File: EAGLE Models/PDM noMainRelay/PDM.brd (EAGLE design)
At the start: 89.7 x 75.6 mm, 20 parts

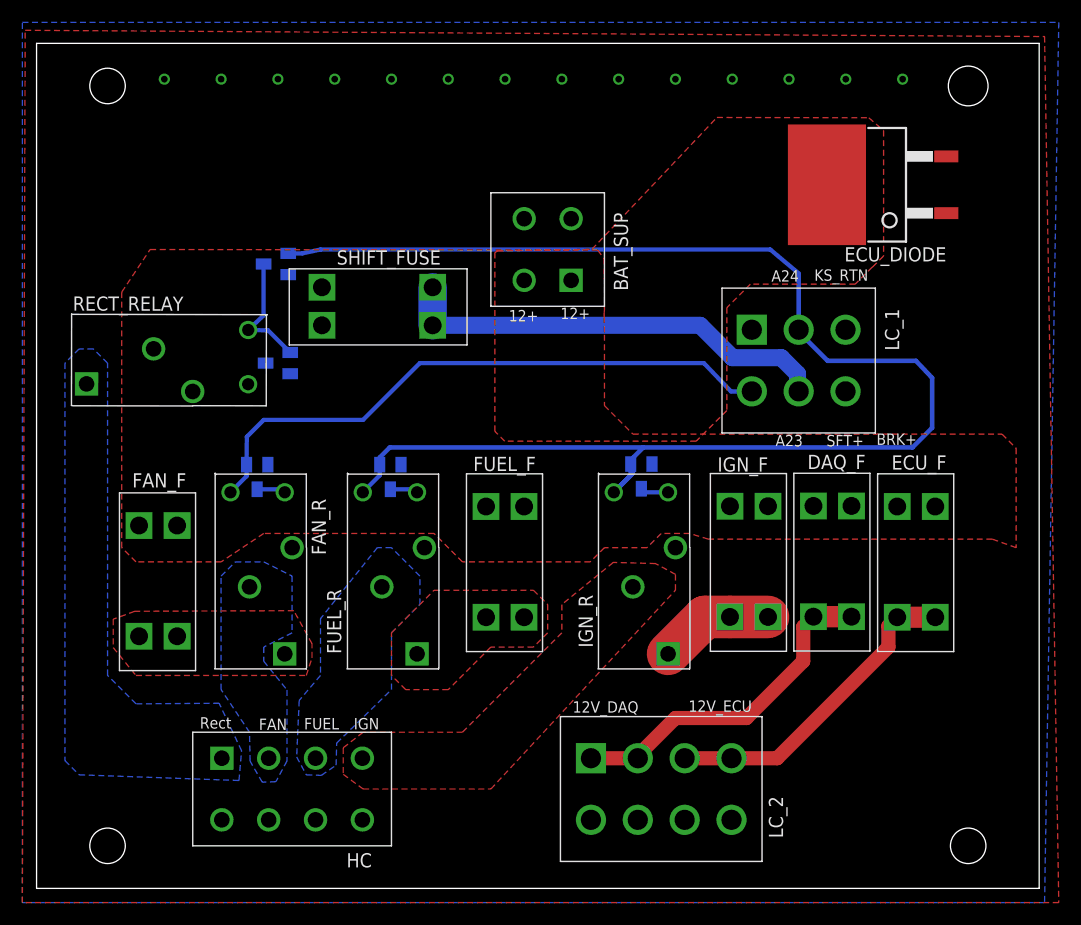
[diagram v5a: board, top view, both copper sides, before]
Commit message: Moved diode
Added different diode
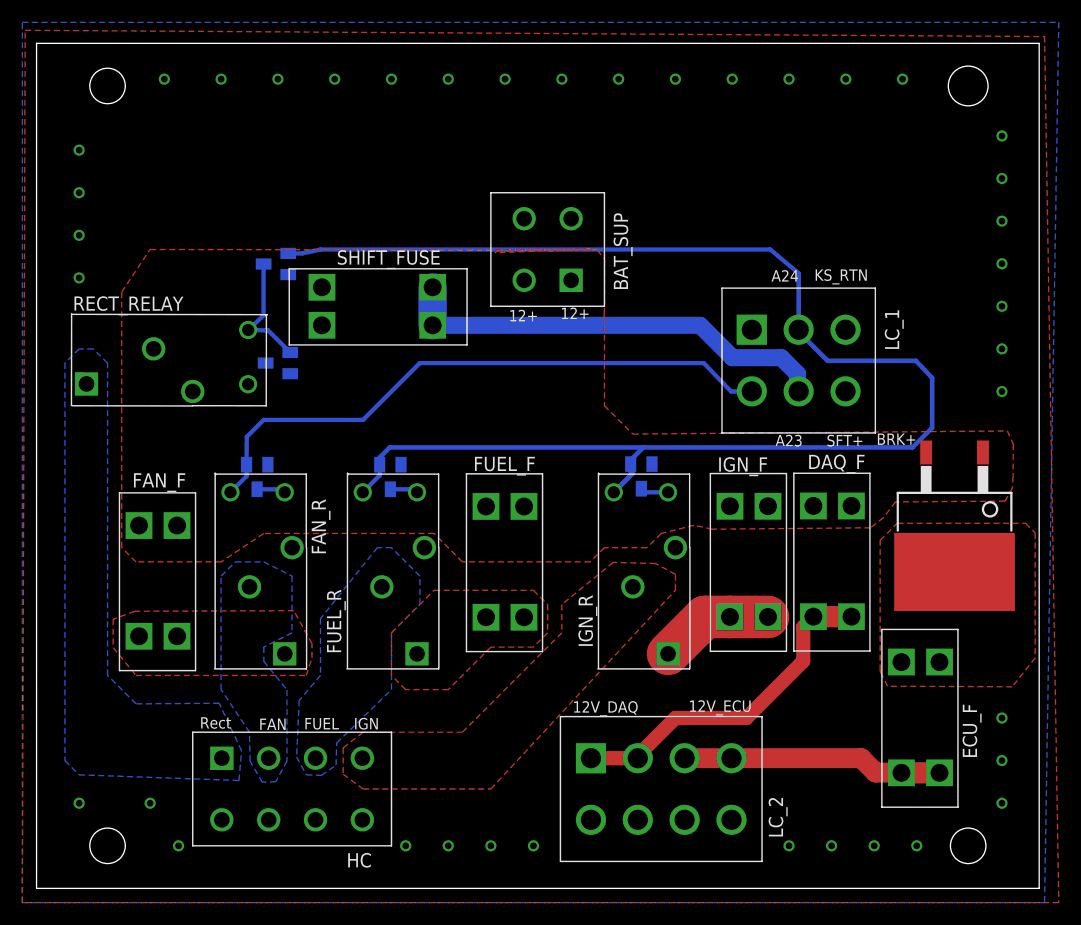
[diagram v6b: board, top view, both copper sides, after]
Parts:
- removed ECU_DIODE: VBT2045BP-E3, vishay:TO-263-3
- added U$1: STPS20L15G-TRTO, st-microelectronics:TO-262DIODE
- moved ECU_F 13.9 mm to (79.1, 15.3)
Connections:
- new net ECU_PROTECTED: ECU_F.1, ECU_F.2, U$1.K
- net 12V: now also U$1.1, U$1.2; no longer ECU_DIODE.K, ECU_F.1, ECU_F.2
- net GND: no longer ECU_DIODE.1, ECU_DIODE.2
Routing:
- net 12V_FUSED_ECU: track 28.7 -> 23.3 mm
- added copper zone on layer 1, net ECU_PROTECTED
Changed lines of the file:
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@@
 <param name="mdViaViaSameLayer" value="8mil"/>
 <param name="mnLayersViaInSmd" value="2"/>
-<param name="mdCopperDimension" value="40mil"/>
+<param name="mdCopperDimension" value="10mil"/>
 <param name="mdDrill" value="8mil"/>
 <param name="mdSmdStop" value="0mil"/>
 <param name="msWidth" value="10mil"/>
-<param name="msDrill" value="20mil"/>
+<param name="msDrill" value="15mil"/>
 <param name="msMicroVia" value="9.99mm"/>
 <param name="msBlindViaRatio" value="0.5"/>
@@
 <element name="IGN_F" library="Keystone" package="3568" value="3568" x="63.7286" y="29.2354" smashed="yes" rot="R270">
 <attribute name="NAME" x="60.9092" y="37.2872" size="1.27" layer="25"/>
-<attribute name="VALUE" x="61.3664" y="31.3436" size="1.27" layer="27"/>
+<attribute name="VALUE" x="61.3918" y="30.6324" size="1.27" layer="27"/>
 </element>
 <element name="FAN_F" library="Keystone" package="3568" value="3568" x="10.8712" y="27.5082" smashed="yes" rot="R270">
@@
 <element name="DAQ_F" library="Keystone" package="3568" value="3568" x="71.1962" y="29.2608" smashed="yes" rot="R270">
 <attribute name="NAME" x="68.961" y="37.5158" size="1.27" layer="25"/>
-<attribute name="VALUE" x="69.5452" y="31.4198" size="1.27" layer="27"/>
+<attribute name="VALUE" x="69.5198" y="31.1912" size="1.27" layer="27"/>
 </element>
 <element name="LC_1" library="BMS Lbr" package="1586041-6" value="1586041-6" x="68.1736" y="47.2186" smashed="yes">
@@
 </element>
 <element name="IGN_D" library="diodes-inc" package="SOT23-3" value="MMBD4448H-7-F" x="54.102" y="36.8554" smashed="yes" rot="MR180">
-<attribute name="NAME" x="51.816" y="40.4368" size="1.27" layer="26" rot="MR180"/>
+<attribute name="NAME" x="51.7652" y="41.6052" size="1.27" layer="26" rot="MR180"/>
 </element>
 <element name="FUEL_D" library="diodes-inc" package="SOT23-3" value="MMBD4448H-7-F" x="31.6484" y="36.8046" smashed="yes" rot="MR180">
-<attribute name="NAME" x="28.3464" y="40.3352" size="1.27" layer="26" rot="MR180"/>
+<attribute name="NAME" x="28.5242" y="40.7162" size="1.27" layer="26" rot="MR180"/>
 </element>
 <element name="FAN_D" library="diodes-inc" package="SOT23-3" value="MMBD4448H-7-F" x="19.7358" y="36.8046" smashed="yes" rot="MR180">
-<attribute name="NAME" x="17.4244" y="40.3352" size="1.27" layer="26" rot="MR180"/>
-</element>
-<element name="ECU_F" library="Keystone" package="3568" value="3568" x="78.6892" y="29.21" smashed="yes" rot="R270">
-<attribute name="NAME" x="76.4794" y="37.465" size="1.27" layer="25"/>
-<attribute name="VALUE" x="77.1398" y="31.3436" size="1.27" layer="27"/>
+<attribute name="NAME" x="17.2974" y="41.2242" size="1.27" layer="26" rot="MR180"/>
+</element>
+<element name="ECU_F" library="Keystone" package="3568" value="3568" x="79.0702" y="15.2908" smashed="yes" rot="R270">
+<attribute name="NAME" x="84.1248" y="11.6078" size="1.27" layer="25" rot="R90"/>
+<attribute name="VALUE" x="77.3684" y="15.5194" size="1.27" layer="27"/>
 </element>
 <element name="CC_D" library="diodes-inc" package="SOT23-3" value="MMBD4448H-7-F" x="21.59" y="46.99" smashed="yes" rot="MR270">
 <attribute name="NAME" x="25.5778" y="48.3108" size="1.27" layer="26" rot="MR270"/>
 </element>
-<element name="ECU_DIODE" library="vishay" package="TO-263-3" value="VBT2045BP-E3" x="76.3016" y="62.9412" rot="R90"/>
+<element name="U$1" library="st-microelectronics" package="TO-262DIODE" value="STPS20L15G-TRTO" x="82.1182" y="33.909" smashed="yes" rot="R180"/>
 </elements>
 <signals>
@@
 <via x="77.47" y="72.39" extent="1-16" drill="0.6"/>
 <contactref element="CC_D" pad="3"/>
-<contactref element="ECU_DIODE" pad="1"/>
-<contactref element="ECU_DIODE" pad="2"/>
+<via x="86.36" y="44.45" extent="1-16" drill="0.6"/>
+<via x="86.36" y="48.26" extent="1-16" drill="0.6"/>
+<via x="86.36" y="52.07" extent="1-16" drill="0.6"/>
+<via x="86.36" y="55.88" extent="1-16" drill="0.6"/>
+<via x="86.36" y="59.69" extent="1-16" drill="0.6"/>
+<via x="86.36" y="15.24" extent="1-16" drill="0.6"/>
+<via x="86.36" y="11.43" extent="1-16" drill="0.6"/>
+<via x="74.93" y="3.81" extent="1-16" drill="0.6"/>
+<via x="71.12" y="3.81" extent="1-16" drill="0.6"/>
+<via x="67.31" y="3.81" extent="1-16" drill="0.6"/>
+<via x="44.45" y="3.81" extent="1-16" drill="0.6"/>
+<via x="40.64" y="3.81" extent="1-16" drill="0.6"/>
+<via x="36.83" y="3.81" extent="1-16" drill="0.6"/>
+<via x="33.02" y="3.81" extent="1-16" drill="0.6"/>
+<via x="12.7" y="3.81" extent="1-16" drill="0.6"/>
+<via x="10.16" y="7.62" extent="1-16" drill="0.6"/>
+<via x="3.81" y="7.62" extent="1-16" drill="0.6"/>
+<via x="86.36" y="7.62" extent="1-16" drill="0.6"/>
+<via x="78.74" y="3.81" extent="1-16" drill="0.6"/>
+<via x="3.81" y="66.04" extent="1-16" drill="0.6"/>
+<via x="3.81" y="62.23" extent="1-16" drill="0.6"/>
+<via x="3.81" y="58.42" extent="1-16" drill="0.6"/>
+<via x="3.81" y="54.61" extent="1-16" drill="0.6"/>
+<via x="86.36" y="63.5" extent="1-16" drill="0.6"/>
+<via x="86.36" y="67.31" extent="1-16" drill="0.6"/>
 </signal>
 <signal name="12V">
@@
 <contactref element="FUEL_D" pad="3"/>
 <contactref element="FAN_D" pad="3"/>
-<contactref element="ECU_F" pad="2"/>
-<contactref element="ECU_F" pad="1"/>
 <wire x1="22.1996" y1="35.433" x2="22.1996" y2="35.8726" width="0.381" layer="16"/>
 <wire x1="54.102" y1="35.7554" x2="54.4244" y2="35.433" width="0.381" layer="16"/>
@@
 <vertex x="10.16" y="57.15"/>
 <vertex x="50.1904" y="57.0992"/>
-<vertex x="50.7746" y="56.3372"/>
+<vertex x="50.8254" y="56.2102"/>
 <vertex x="50.8" y="51.7652"/>
 <vertex x="50.7746" y="51.5112"/>
@@
 <vertex x="50.8" y="43.18"/>
 <vertex x="53.34" y="40.64"/>
-<vertex x="86.36" y="40.64"/>
-<vertex x="87.63" y="39.37"/>
-<vertex x="87.63" y="30.48"/>
-<vertex x="85.4964" y="31.242"/>
-<vertex x="60.0964" y="31.242"/>
-<vertex x="58.42" y="31.75"/>
+<vertex x="86.8426" y="40.9194"/>
+<vertex x="87.376" y="39.7256"/>
+<vertex x="87.3506" y="36.83"/>
+<vertex x="87.2998" y="35.8394"/>
+<vertex x="86.6394" y="34.6456"/>
+<vertex x="76.835" y="34.5694"/>
+<vertex x="75.7682" y="33.1724"/>
+<vertex x="74.5998" y="32.258"/>
+<vertex x="60.4266" y="32.131"/>
+<vertex x="58.8264" y="32.4866"/>
 <vertex x="55.88" y="31.75"/>
 <vertex x="54.61" y="30.48"/>
@@
 </polygon>
 <wire x1="42.9973" y1="54.3941" x2="43.61941875" y2="54.3941" width="0.4064" layer="1"/>
-<contactref element="ECU_DIODE" pad="K"/>
 <polygon width="0.4064" layer="1">
 <vertex x="41.2242" y="57.023"/>
 <vertex x="49.6824" y="57.1754"/>
-<vertex x="60.8584" y="68.961"/>
-<vertex x="74.4474" y="68.9356"/>
-<vertex x="75.7682" y="67.7926"/>
-<vertex x="75.7682" y="56.5658"/>
-<vertex x="74.7776" y="55.5752"/>
-<vertex x="74.7522" y="55.5752"/>
-<vertex x="73.2282" y="54.0512"/>
-<vertex x="63.8556" y="54.0512"/>
-<vertex x="61.7474" y="51.943"/>
-<vertex x="61.7474" y="42.7482"/>
-<vertex x="59.0042" y="40.005"/>
-<vertex x="41.8846" y="40.005"/>
-<vertex x="40.9956" y="40.894"/>
 <vertex x="40.9956" y="56.8706"/>
 </polygon>
+<contactref element="U$1" pad="1"/>
+<contactref element="U$1" pad="2"/>
 </signal>
 <signal name="12V_FUSED_ECU">
@@
 <contactref element="LC_2" pad="4"/>
 <contactref element="LC_2" pad="3"/>
-<wire x1="76.9874" y1="24.257" x2="80.391" y2="24.257" width="1.905" layer="1"/>
-<wire x1="57.9755" y1="11.6459" x2="62.1665" y2="11.6459" width="1.27" layer="1"/>
-<wire x1="62.1665" y1="11.6459" x2="66.2559" y2="11.6459" width="1.27" layer="1"/>
-<wire x1="66.2559" y1="11.6459" x2="76.2" y2="21.59" width="1.27" layer="1"/>
-<wire x1="76.2" y1="21.59" x2="76.2" y2="23.4696" width="1.27" layer="1"/>
-<wire x1="76.2" y1="23.4696" x2="76.9874" y2="24.257" width="1.27" layer="1"/>
+<wire x1="77.3684" y1="10.3378" x2="80.772" y2="10.3378" width="1.905" layer="1"/>
+<wire x1="57.9755" y1="11.6459" x2="62.1665" y2="11.6459" width="1.778" layer="1"/>
+<wire x1="62.1665" y1="11.6459" x2="73.7743" y2="11.6459" width="1.778" layer="1"/>
+<wire x1="73.7743" y1="11.6459" x2="75.057" y2="10.3632" width="1.778" layer="1"/>
+<wire x1="75.057" y1="10.3632" x2="77.343" y2="10.3632" width="1.778" layer="1"/>
+<wire x1="77.343" y1="10.3632" x2="77.3684" y2="10.3378" width="1.778" layer="1"/>
 </signal>
 <signal name="KILL_SWITCH_DIODE">
@@
 <wire x1="68.1736" y1="49.784" x2="70.7644" y2="47.1932" width="0.4064" layer="16"/>
 </signal>
+<signal name="ECU_PROTECTED">
+<contactref element="ECU_F" pad="1"/>
+<contactref element="ECU_F" pad="2"/>
+<contactref element="U$1" pad="K"/>
+<polygon width="0.4064" layer="1" thermals="no">
+<vertex x="75.4634" y="31.1404"/>
+<vertex x="76.962" y="32.639"/>
+<vertex x="76.9874" y="32.639"/>
+<vertex x="77.0128" y="32.6644"/>
+<vertex x="88.4682" y="32.6644"/>
+<vertex x="89.3318" y="31.8008"/>
+<vertex x="89.3318" y="20.6248"/>
+<vertex x="87.2744" y="18.034"/>
+<vertex x="76.1238" y="18.0848"/>
+<vertex x="75.6158" y="19.1008"/>
+<vertex x="75.438" y="19.4818"/>
+<vertex x="75.4634" y="19.5072"/>
+</polygon>
+</signal>
 </signals>
